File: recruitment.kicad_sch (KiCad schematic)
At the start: 10 parts

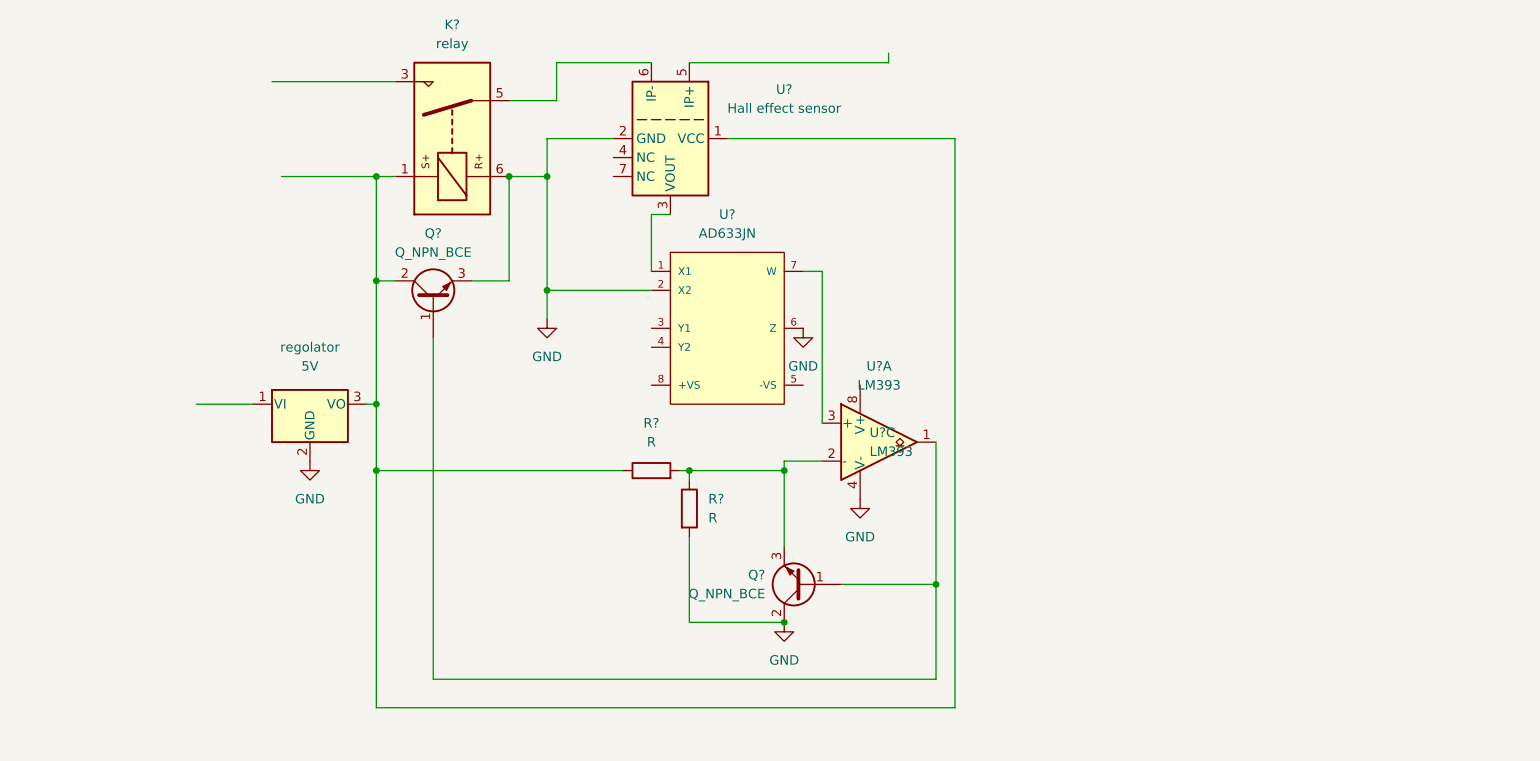
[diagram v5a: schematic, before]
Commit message: add R values, TODO: understand transistors
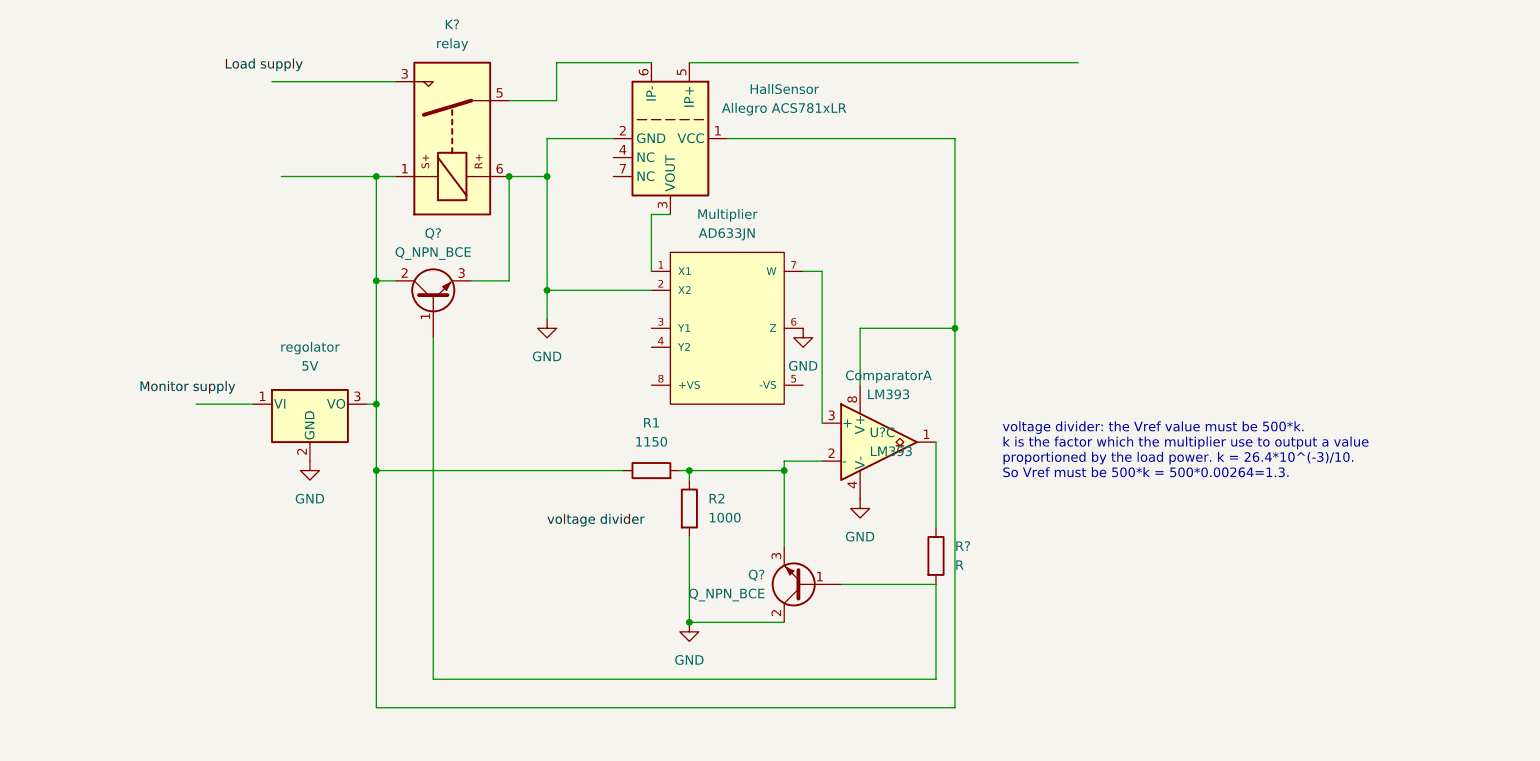
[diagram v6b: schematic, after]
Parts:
- added R?: R, symbol Device:R
- HallSensor: renamed from U?; value Hall effect sensor -> Allegro ACS781xLR
- R1: renamed from R?; value R -> 1150
- R2: renamed from R?; value R -> 1000
- gave numbers to parts that had none: 2
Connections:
- net at HallSensor.1 (VCC), K?.1, Q?.2 (C)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: now also U?.8 (V+)
- net at Q?.1 (B), Q?.1 (B): now also R?.2; no longer Comparator.1
- new net: Comparator.1, R?.1
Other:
- note added: "voltage divider: the Vref value must be 500*k. k is the factor which the multiplier use to output a value proportioned by the load power. k = 26.4*10^(-3)/10. So Vref must be 500*k = 500*0.00264=1.3."
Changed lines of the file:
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@@
   (junction (at 140.97 69.85) (diameter 0) (color 0 0 0 0)
   )
-  (junction (at 172.72 129.54) (diameter 0) (color 0 0 0 0)
+  (junction (at 195.58 90.17) (diameter 0) (color 0 0 0 0)
   )
   (junction (at 140.97 85.09) (diameter 0) (color 0 0 0 0)
@@
   (junction (at 118.11 83.82) (diameter 0) (color 0 0 0 0)
   )
-  (junction (at 193.04 124.46) (diameter 0) (color 0 0 0 0)
+  (junction (at 160.02 129.54) (diameter 0) (color 0 0 0 0)
   )
   (wire (pts (xy 180.34 124.46) (xy 193.04 124.46))
@@
     (stroke (width 0) (type default) (color 0 0 0 0))
   )
-  (wire (pts (xy 160.02 54.61) (xy 186.69 54.61))
+  (wire (pts (xy 160.02 54.61) (xy 212.09 54.61))
     (stroke (width 0) (type default) (color 0 0 0 0))
   )
@@
     (stroke (width 0) (type default) (color 0 0 0 0))
   )
-  (wire (pts (xy 193.04 124.46) (xy 193.04 105.41))
-    (stroke (width 0) (type default) (color 0 0 0 0))
-  )
   (wire (pts (xy 149.86 64.77) (xy 140.97 64.77))
     (stroke (width 0) (type default) (color 0 0 0 0))
@@
     (stroke (width 0) (type default) (color 0 0 0 0))
   )
+  (wire (pts (xy 195.58 90.17) (xy 195.58 140.97))
+    (stroke (width 0) (type default) (color 0 0 0 0))
+  )
   (wire (pts (xy 130.81 83.82) (xy 135.89 83.82))
     (stroke (width 0) (type default) (color 0 0 0 0))
@@
     (stroke (width 0) (type default) (color 0 0 0 0))
   )
+  (wire (pts (xy 193.04 105.41) (xy 193.04 116.84))
+    (stroke (width 0) (type default) (color 0 0 0 0))
+  )
+  (wire (pts (xy 182.88 90.17) (xy 195.58 90.17))
+    (stroke (width 0) (type default) (color 0 0 0 0))
+  )
   (wire (pts (xy 118.11 83.82) (xy 118.11 69.85))
     (stroke (width 0) (type default) (color 0 0 0 0))
   )
-  (wire (pts (xy 195.58 64.77) (xy 195.58 140.97))
+  (wire (pts (xy 195.58 64.77) (xy 195.58 90.17))
     (stroke (width 0) (type default) (color 0 0 0 0))
   )
@@
     (stroke (width 0) (type default) (color 0 0 0 0))
   )
-  (wire (pts (xy 186.69 53.34) (xy 186.69 54.61))
+  (wire (pts (xy 182.88 97.79) (xy 182.88 90.17))
     (stroke (width 0) (type default) (color 0 0 0 0))
   )
@@
     (stroke (width 0) (type default) (color 0 0 0 0))
   )
+  (text "voltage divider: the Vref value must be 500*k.\nk is the factor which the multiplier use to output a value\nproportioned by the load power. k = 26.4*10^(-3)/10.\nSo Vref must be 500*k = 500*0.00264=1.3."
+    (at 201.93 110.49 0)
+    (effects (font (size 1.27 1.27)) (justify left bottom))
+  )
+  (label "Load supply" (at 97.79 55.88 0)
+    (effects (font (size 1.27 1.27)) (justify left bottom))
+  )
+  (label "Monitor supply" (at 86.36 99.06 0)
+    (effects (font (size 1.27 1.27)) (justify left bottom))
+  )
+  (label "voltage divider" (at 140.97 116.84 0)
+    (effects (font (size 1.27 1.27)) (justify left bottom))
+  )
   (symbol (lib_id "Device:R") (at 160.02 114.3 0) (unit 1)
     (in_bom yes) (on_board yes) (fields_autoplaced)
-    (property "Reference" "R?" (id 0) (at 162.56 113.0299 0)
-      (effects (font (size 1.27 1.27)) (justify left))
-    )
-    (property "Value" "R" (id 1) (at 162.56 115.5699 0)
+    (property "Reference" "R2" (id 0) (at 162.56 113.0299 0)
+      (effects (font (size 1.27 1.27)) (justify left))
+    )
+    (property "Value" "1000" (id 1) (at 162.56 115.5699 0)
       (effects (font (size 1.27 1.27)) (justify left))
     )
@@
   (symbol (lib_id "Sensor_Current:ACS781xLRTR-050B") (at 157.48 64.77 270) (unit 1)
     (in_bom yes) (on_board yes) (fields_autoplaced)
-    (property "Reference" "U?" (id 0) (at 172.72 58.1912 90))
-    (property "Value" "Hall effect sensor" (id 1) (at 172.72 60.7312 90))
+    (property "Reference" "HallSensor" (id 0) (at 172.72 58.1912 90))
+    (property "Value" "Allegro ACS781xLR" (id 1) (at 172.72 60.7312 90))
     (property "Footprint" "Sensor_Current:Allegro_PSOF-7_4.8x6.4mm_P1.60mm" (id 2) (at 157.48 64.77 0)
       (effects (font (size 1.27 1.27)) hide)
@@
     (pin "7")
   )
+  (symbol (lib_id "Device:R") (at 193.04 120.65 0) (unit 1)
+    (in_bom yes) (on_board yes) (fields_autoplaced)
+    (property "Reference" "R?" (id 0) (at 195.58 119.3799 0)
+      (effects (font (size 1.27 1.27)) (justify left))
+    )
+    (property "Value" "R" (id 1) (at 195.58 121.9199 0)
+      (effects (font (size 1.27 1.27)) (justify left))
+    )
+    (property "Footprint" "" (id 2) (at 191.262 120.65 90)
+      (effects (font (size 1.27 1.27)) hide)
+    )
+    (property "Datasheet" "~" (id 3) (at 193.04 120.65 0)
+      (effects (font (size 1.27 1.27)) hide)
+    )
+    (pin "1")
+    (pin "2")
+  )
   (symbol (lib_id "eec:AD633JN") (at 152.4 82.55 0) (unit 1)
     (in_bom yes) (on_board yes) (fields_autoplaced)
-    (property "Reference" "U?" (id 0) (at 165.1 74.93 0))
+    (property "Reference" "Multiplier" (id 0) (at 165.1 74.93 0))
     (property "Value" "AD633JN" (id 1) (at 165.1 77.47 0))
     (property "Footprint" "Analog_Devices-AD633JN-*" (id 2) (at 152.4 72.39 0)
@@
   (symbol (lib_id "Device:R") (at 154.94 109.22 90) (unit 1)
     (in_bom yes) (on_board yes) (fields_autoplaced)
-    (property "Reference" "R?" (id 0) (at 154.94 102.87 90))
-    (property "Value" "R" (id 1) (at 154.94 105.41 90))
+    (property "Reference" "R1" (id 0) (at 154.94 102.87 90))
+    (property "Value" "1150" (id 1) (at 154.94 105.41 90))
     (property "Footprint" "" (id 2) (at 154.94 110.998 90)
       (effects (font (size 1.27 1.27)) hide)
@@
     (pin "2")
   )
-  (symbol (lib_id "power:GND") (at 172.72 129.54 0) (unit 1)
-    (in_bom yes) (on_board yes) (fields_autoplaced)
-    (property "Reference" "#PWR?" (id 0) (at 172.72 135.89 0)
-      (effects (font (size 1.27 1.27)) hide)
-    )
-    (property "Value" "GND" (id 1) (at 172.72 134.62 0))
-    (property "Footprint" "" (id 2) (at 172.72 129.54 0)
-      (effects (font (size 1.27 1.27)) hide)
-    )
-    (property "Datasheet" "" (id 3) (at 172.72 129.54 0)
+  (symbol (lib_id "power:GND") (at 160.02 129.54 0) (unit 1)
+    (in_bom yes) (on_board yes) (fields_autoplaced)
+    (property "Reference" "#PWR?" (id 0) (at 160.02 135.89 0)
+      (effects (font (size 1.27 1.27)) hide)
+    )
+    (property "Value" "GND" (id 1) (at 160.02 134.62 0))
+    (property "Footprint" "" (id 2) (at 160.02 129.54 0)
+      (effects (font (size 1.27 1.27)) hide)
+    )
+    (property "Datasheet" "" (id 3) (at 160.02 129.54 0)
       (effects (font (size 1.27 1.27)) hide)
     )
@@
   )
   (symbol (lib_id "Comparator:LM393") (at 185.42 105.41 0) (unit 1)
-    (in_bom yes) (on_board yes) (fields_autoplaced)
-    (property "Reference" "U?" (id 0) (at 185.42 95.25 0))
-    (property "Value" "LM393" (id 1) (at 185.42 97.79 0))
+    (in_bom yes) (on_board yes)
+    (property "Reference" "Comparator" (id 0) (at 186.69 96.52 0))
+    (property "Value" "LM393" (id 1) (at 186.69 99.06 0))
     (property "Footprint" "" (id 2) (at 185.42 105.41 0)
       (effects (font (size 1.27 1.27)) hide)
@@
       (reference "#PWR?") (unit 1) (value "GND") (footprint "")
     )
+    (path "/e6e45776-f57c-4519-a99b-28f22f45c493"
+      (reference "Comparator") (unit 1) (value "LM393") (footprint "")
+    )
+    (path "/1b77c8f9-b0fa-45ba-a726-522a68924cf1"
+      (reference "HallSensor") (unit 1) (value "Allegro ACS781xLR") (footprint "Sensor_Current:Allegro_PSOF-7_4.8x6.4mm_P1.60mm")
+    )
     (path "/b4450c83-6da6-4393-a892-92bf8cbec8aa"
       (reference "K?") (unit 1) (value "relay") (footprint "Relay_THT:Relay_1P1T_NO_10x24x18.8mm_Panasonic_ADW11xxxxW_THT")
     )
+    (path "/394656a1-8b92-4995-815f-d107d37664e0"
+      (reference "Multiplier") (unit 1) (value "AD633JN") (footprint "Analog_Devices-AD633JN-*")
+    )
     (path "/c28069b2-6ad3-4558-8513-38d165d26da9"
       (reference "Q?") (unit 1) (value "Q_NPN_BCE") (footprint "")
@@
       (reference "Q?") (unit 1) (value "Q_NPN_BCE") (footprint "")
     )
+    (path "/424d5b31-88ca-4b43-8316-4aec53e16753"
+      (reference "R1") (unit 1) (value "1150") (footprint "")
+    )
     (path "/0688bc70-7f53-41de-a6b4-1297b52069e5"
+      (reference "R2") (unit 1) (value "1000") (footprint "")
+    )
+    (path "/2b884f0d-0495-4eec-a050-722975269cbc"
       (reference "R?") (unit 1) (value "R") (footprint "")
     )
-    (path "/424d5b31-88ca-4b43-8316-4aec53e16753"
-      (reference "R?") (unit 1) (value "R") (footprint "")
-    )
-    (path "/1b77c8f9-b0fa-45ba-a726-522a68924cf1"
-      (reference "U?") (unit 1) (value "Hall effect sensor") (footprint "Sensor_Current:Allegro_PSOF-7_4.8x6.4mm_P1.60mm")
-    )
-    (path "/394656a1-8b92-4995-815f-d107d37664e0"
-      (reference "U?") (unit 1) (value "AD633JN") (footprint "Analog_Devices-AD633JN-*")
-    )
-    (path "/e6e45776-f57c-4519-a99b-28f22f45c493"
-      (reference "U?") (unit 1) (value "LM393") (footprint "")
-    )
     (path "/7e297a54-659a-4701-a7f4-aec0b895b712"

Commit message: add switch, TODO: check loop transistor
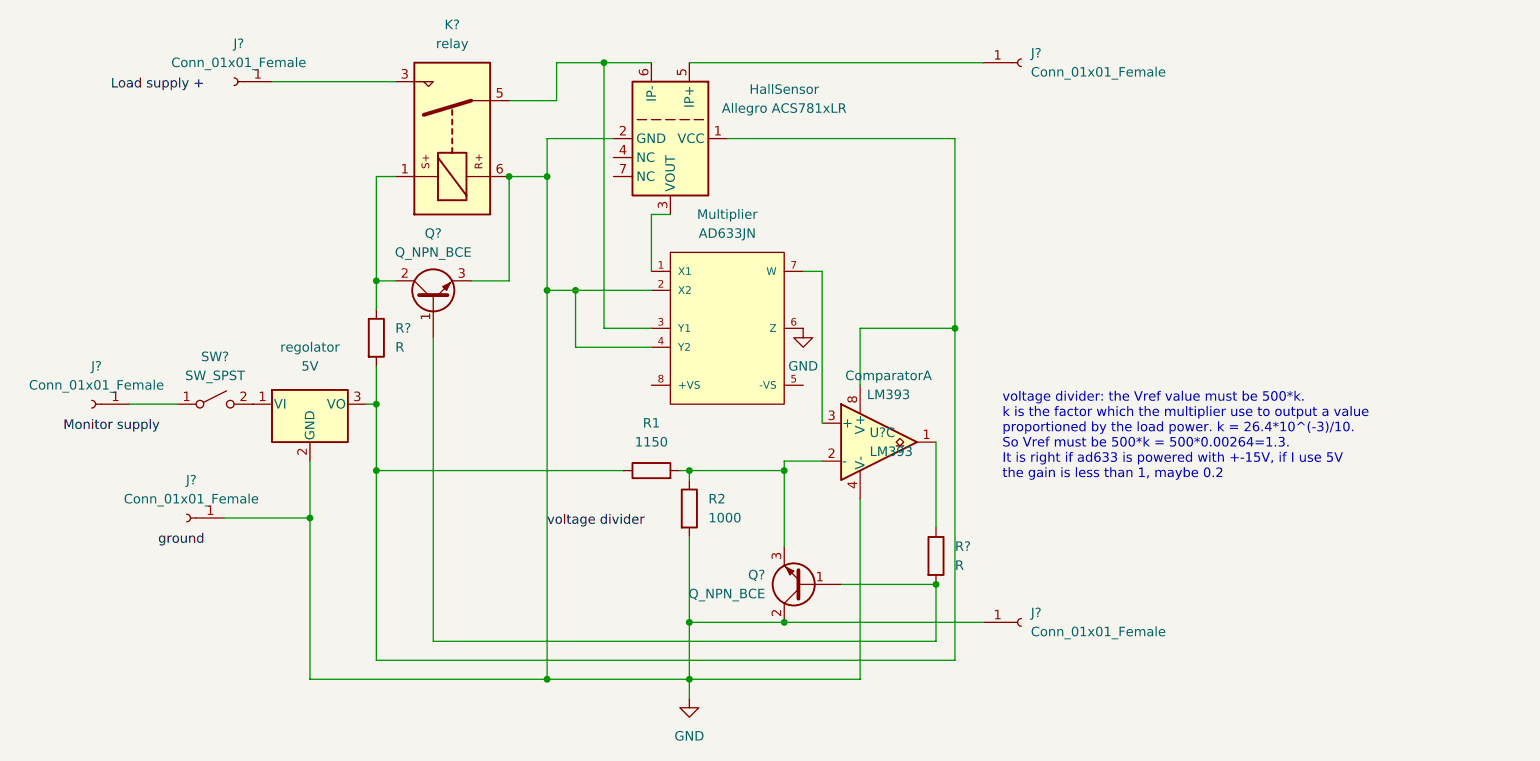
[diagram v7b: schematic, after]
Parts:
- added J? (x5): Conn_01x01_Female, symbol Connector:Conn_01x01_Female
- added R?: R, symbol Device:R
- added SW?: SW_SPST, symbol Switch:SW_SPST
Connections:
- net GND: now also Multiplier.4 (Y2), J?.1 (Pin_1), J?.1 (Pin_1)
- net at HallSensor.1 (VCC), R1.1, U?.8 (V+)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: now also R?.2; no longer K?.1, Q?.2 (C)
- net at HallSensor.5 (IP+): now also J?.1 (Pin_1)
- net at HallSensor.6 (IP-), K?.5: now also Multiplier.3 (Y1)
- net at regolator.1 (VI): now also SW?.2 (B)
- net at K?.3: now also J?.1 (Pin_1)
- new net: K?.1, Q?.2 (C), R?.1
- new net: J?.1 (Pin_1), SW?.1 (A)
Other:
- note added: "voltage divider: the Vref value must be 500*k. k is the factor which the multiplier use to output a value proportioned by the load power. k = 26.4*10^(-3)/10. So Vref must be 500*k = 500*0.00264=1.3. It is right if ad633 is powered with +-15V, if I use 5V the gain is less than 1, maybe 0.2"
- note removed: "voltage divider: the Vref value must be 500*k. k is the factor which the multiplier use to output a value proportioned by the load power. k = 26.4*10^(-3)/10. So Vref must be 500*k = 500*0.00264=1.3."
